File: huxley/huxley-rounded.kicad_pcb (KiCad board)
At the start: 4 copper layers, 124 x 124 mm, 166 parts, among them J1 CT3151V1-2, J11 SMA_RF2-04A-T-00-50-G, J13 SMA_RF2-04A-T-00-50-G, J15 SMA_RF2-04A-T-00-50-G, J17 SMA_RF2-04A-T-00-50-G, J18 SMA_RF2-04A-T-00-50-G, J19 SMA_RF2-04A-T-00-50-G, J2 CT3151V1-2, J20 SMA_RF2-04A-T-00-50-G, J21 61300211121, J22 SMA_RF2-04A-T-00-50-G, J24 CT3151V1-2, J25 61300211121, J26 61300211121, J27 61300211121, J28 61300211121, J29 61300211121, J3 CT3151V1-2, J30 61300211121, J31 61300211121, J32 61300211121, J34 CT3151V1-0, J35 CT3151V1-2, J37 CT3151V1-0, J39 CT3151V1-2, J4 SMA_RF2-04A-T-00-50-G, J5 SMA_RF2-04A-T-00-50-G, J7 SMA_RF2-04A-T-00-50-G, J9 SMA_RF2-04A-T-00-50-G, U2 LM134H, U3 MAX40201FAUA+, U4 TMUX1112PWR, U5 TMUX1112PWR, U6 NVT2010PW_118

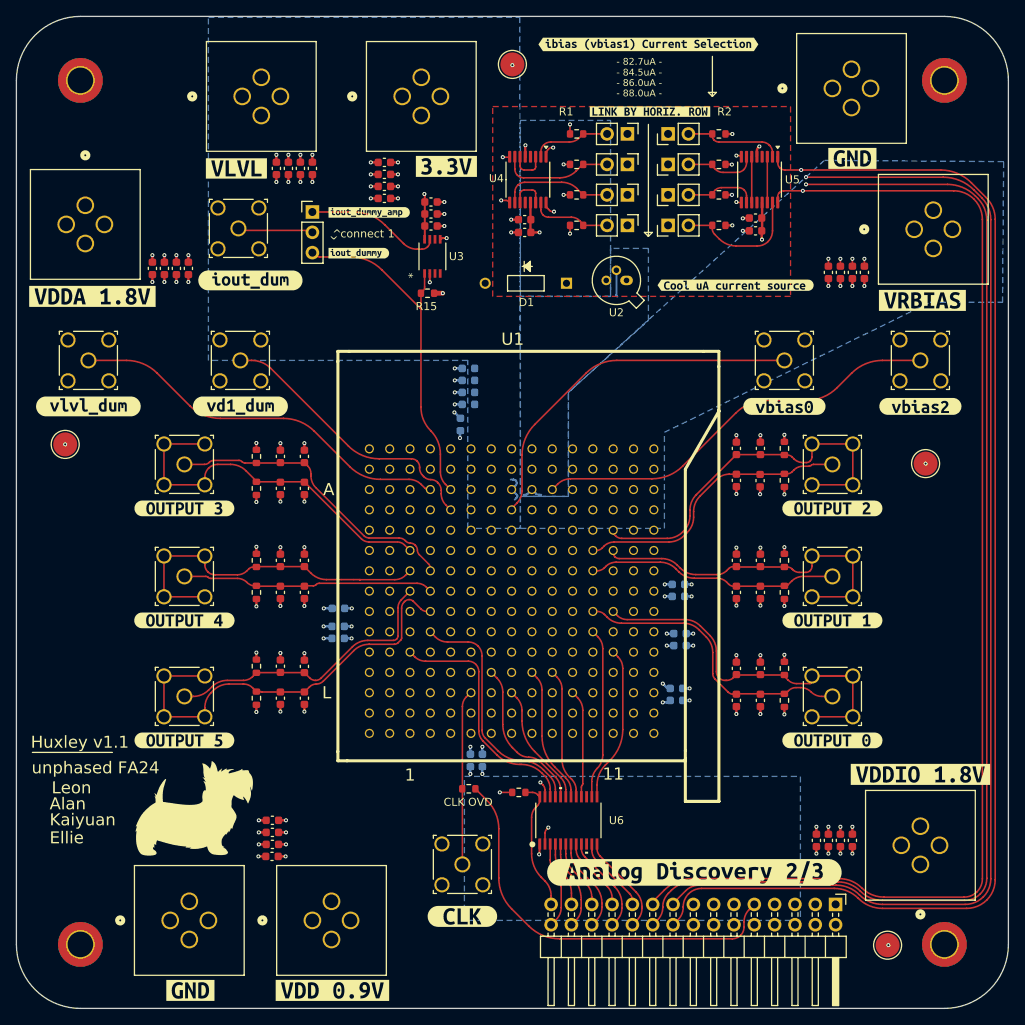
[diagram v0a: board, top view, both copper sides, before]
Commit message: DFA fixes; bump huxley version number to v1.1.1; added updated BOM v1.1.1
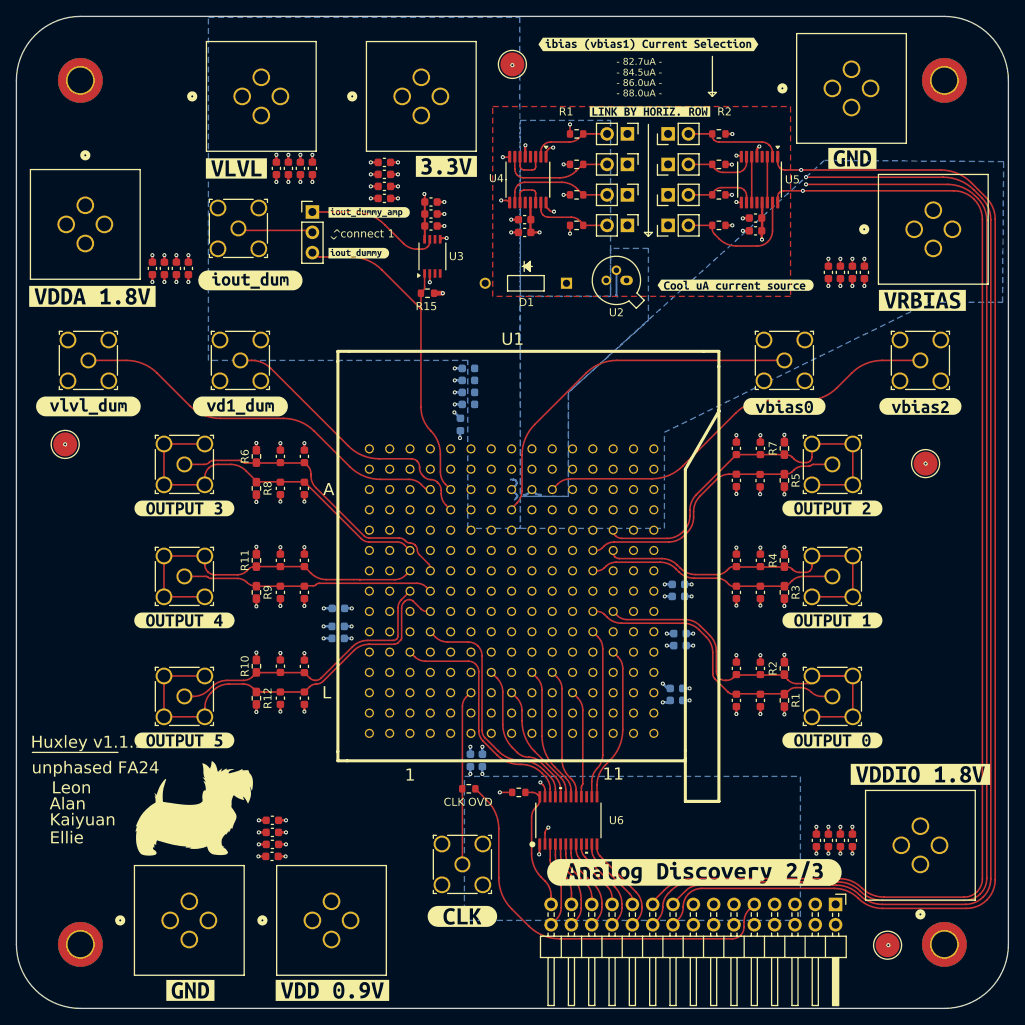
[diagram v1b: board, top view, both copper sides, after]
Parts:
- R1, R10, R11, R12, R2, R3, R4, R5, R6, R7, R8, R9: footprint Resistor_SMD:R_0603_1608Metric -> 0_726_footprints:R_0603_1608Metric_Vishay_WBT
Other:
- board text added: "Huxley v1.1.1"
- board text removed: "Huxley v1.1"
